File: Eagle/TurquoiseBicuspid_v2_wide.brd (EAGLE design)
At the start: 56 x 56 mm, 19 parts, among them J0 0Ω, J2 0Ω

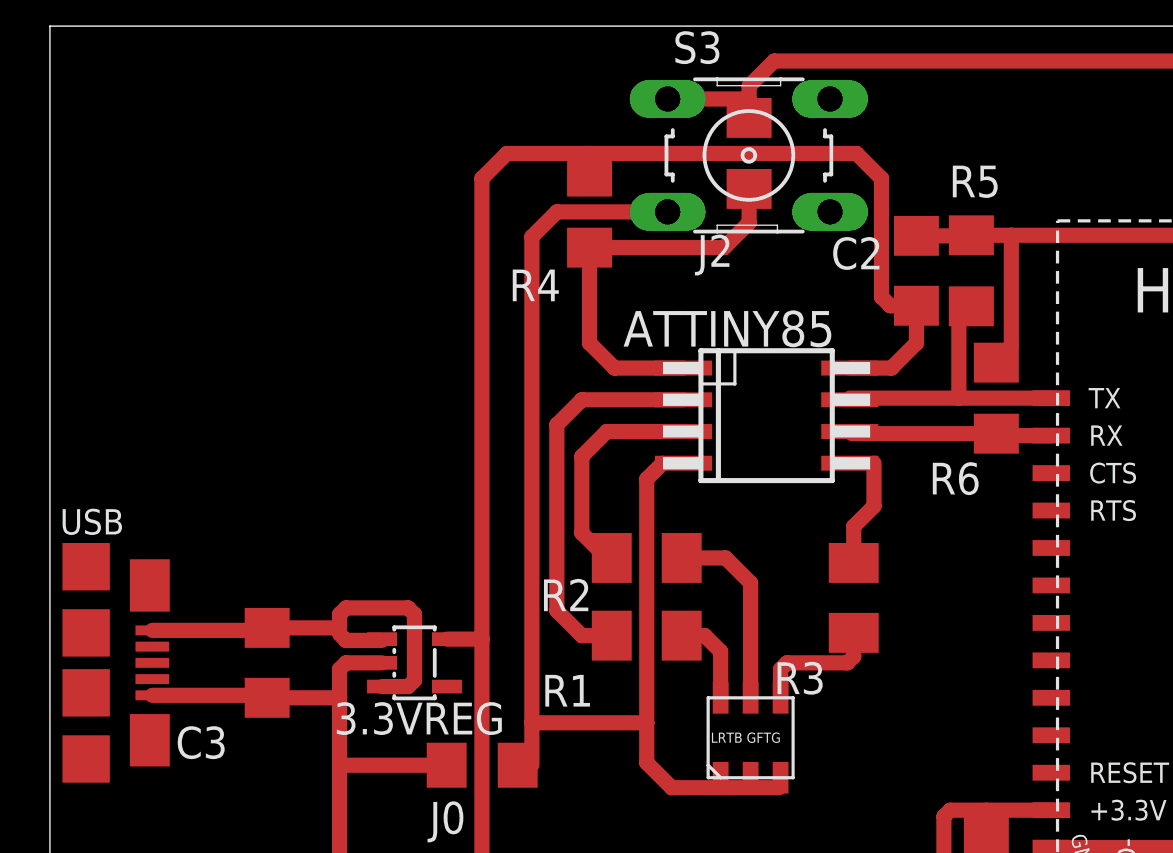
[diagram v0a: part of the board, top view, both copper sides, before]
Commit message: .6mm to .4mm usb
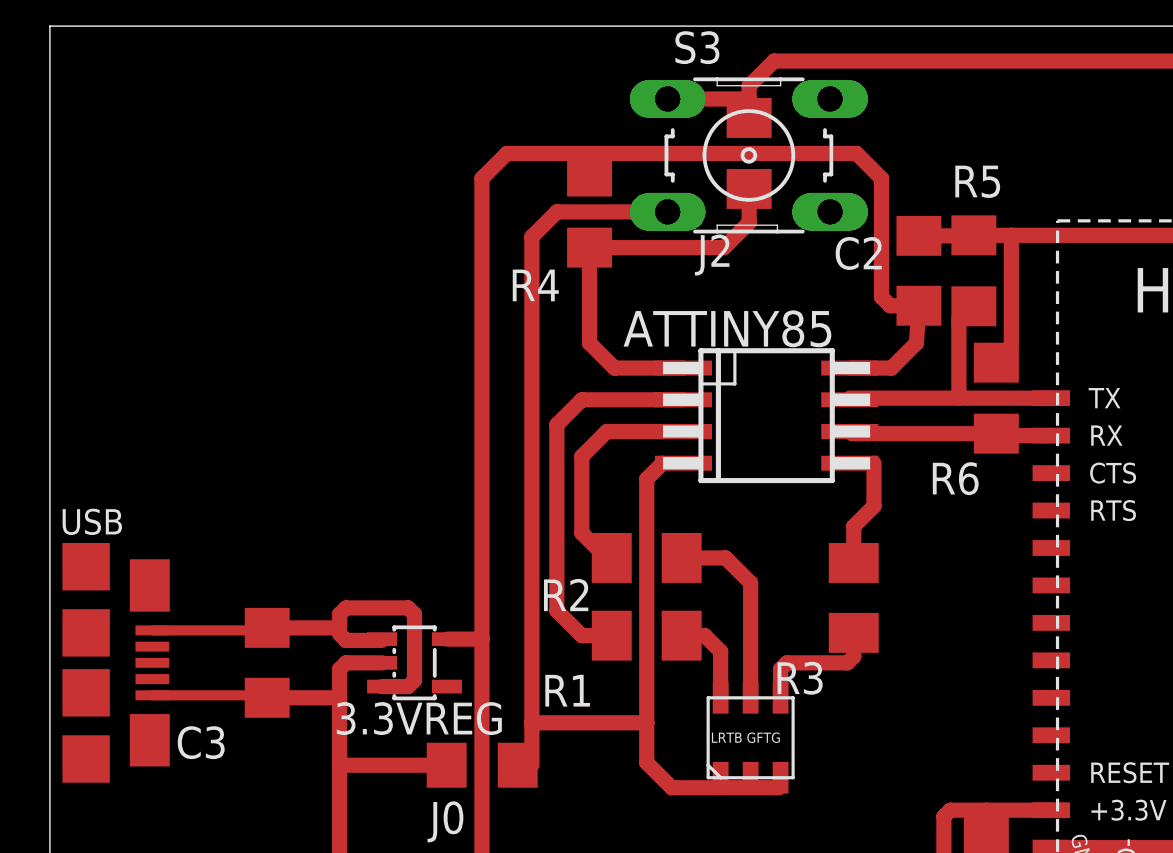
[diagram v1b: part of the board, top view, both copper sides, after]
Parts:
- moved R5 0.10 mm to (37.0, 46.2)
- moved C2 0.10 mm to (34.8, 46.2)
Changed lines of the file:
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@@
 </class>
 </classes>
-<designrules name="default">
+<designrules name="default *">
 <description language="de">&lt;b&gt;EAGLE Design Rules&lt;/b&gt;
 &lt;p&gt;
@@
 <param name="mtCopper" value="0.035mm 0.035mm 0.035mm 0.035mm 0.035mm 0.035mm 0.035mm 0.035mm 0.035mm 0.035mm 0.035mm 0.035mm 0.035mm 0.035mm 0.035mm 0.035mm"/>
 <param name="mtIsolate" value="1.5mm 0.15mm 0.2mm 0.15mm 0.2mm 0.15mm 0.2mm 0.15mm 0.2mm 0.15mm 0.2mm 0.15mm 0.2mm 0.15mm 0.2mm"/>
-<param name="mdWireWire" value="8mil"/>
-<param name="mdWirePad" value="8mil"/>
-<param name="mdWireVia" value="8mil"/>
-<param name="mdPadPad" value="8mil"/>
-<param name="mdPadVia" value="8mil"/>
-<param name="mdViaVia" value="8mil"/>
-<param name="mdSmdPad" value="8mil"/>
-<param name="mdSmdVia" value="8mil"/>
-<param name="mdSmdSmd" value="8mil"/>
+<param name="mdWireWire" value="10mil"/>
+<param name="mdWirePad" value="10mil"/>
+<param name="mdWireVia" value="10mil"/>
+<param name="mdPadPad" value="10mil"/>
+<param name="mdPadVia" value="10mil"/>
+<param name="mdViaVia" value="10mil"/>
+<param name="mdSmdPad" value="10mil"/>
+<param name="mdSmdVia" value="10mil"/>
+<param name="mdSmdSmd" value="10mil"/>
 <param name="mdViaViaSameLayer" value="8mil"/>
 <param name="mnLayersViaInSmd" value="2"/>
@@
 <attribute name="VALUE" x="29.87" y="47.64" size="1.27" layer="27" rot="R180"/>
 </element>
-<element name="R5" library="resistor" package="R1206" value="10kΩ" x="36.9" y="46.2" smashed="yes" rot="R270">
-<attribute name="NAME" x="36.003" y="49.143" size="1.27" layer="25"/>
-<attribute name="VALUE" x="38.403" y="49.187" size="1.27" layer="27"/>
+<element name="R5" library="resistor" package="R1206" value="10kΩ" x="37" y="46.2" smashed="yes" rot="R270">
+<attribute name="NAME" x="36.103" y="49.143" size="1.27" layer="25"/>
+<attribute name="VALUE" x="38.503" y="49.187" size="1.27" layer="27"/>
 </element>
 <element name="R6" library="resistor" package="R1206" value="10kΩ" x="37.9" y="41.1" smashed="yes" rot="R270">
@@
 <attribute name="VALUE" x="21.56" y="36.2042" size="1.4224" layer="27" ratio="9"/>
 </element>
-<element name="C2" library="rcl" package="C1206" value="0.1µf" x="34.7" y="46.2" smashed="yes" rot="R90">
-<attribute name="NAME" x="33.37" y="47.53" size="1.27" layer="25" rot="R180"/>
-<attribute name="VALUE" x="33.77" y="46.14" size="1.27" layer="27" rot="R180"/>
+<element name="C2" library="rcl" package="C1206" value="0.1µf" x="34.8" y="46.2" smashed="yes" rot="R90">
+<attribute name="NAME" x="33.47" y="47.53" size="1.27" layer="25" rot="R180"/>
+<attribute name="VALUE" x="33.87" y="46.14" size="1.27" layer="27" rot="R180"/>
 </element>
 <element name="C3" library="rcl" package="C1206" value="10µf" x="8.7" y="30.5" smashed="yes" rot="R270">
@@
 <contactref element="USB" pad="1"/>
 <contactref element="C3" pad="1"/>
-<wire x1="4.1" y1="31.8" x2="8.6" y2="31.8" width="0.6096" layer="1"/>
+<wire x1="4.1" y1="31.8" x2="8.6" y2="31.8" width="0.4064" layer="1"/>
 <wire x1="8.6" y1="31.8" x2="8.7" y2="31.9" width="0.4064" layer="1"/>
 <wire x1="8.7" y1="31.9" x2="11.6" y2="31.9" width="0.6096" layer="1"/>
@@
 <contactref element="R6" pad="1"/>
 <contactref element="R5" pad="1"/>
-<wire x1="4.1" y1="29.2" x2="8.6" y2="29.2" width="0.6096" layer="1"/>
+<wire x1="4.1" y1="29.2" x2="8.6" y2="29.2" width="0.4064" layer="1"/>
 <wire x1="8.6" y1="29.2" x2="8.7" y2="29.1" width="0.4064" layer="1"/>
 <wire x1="8.7" y1="29.1" x2="11.6" y2="29.1" width="0.6096" layer="1"/>
@@
 <wire x1="6.4" y1="4.1" x2="42.593528125" y2="4.1" width="0.6096" layer="1"/>
 <wire x1="38.4" y1="43.122" x2="38.5" y2="43.222" width="0.4064" layer="1"/>
-<wire x1="34.7" y1="47.6" x2="36.878" y2="47.6" width="0.6096" layer="1"/>
-<wire x1="36.878" y1="47.6" x2="36.9" y2="47.622" width="0.4064" layer="1"/>
-<wire x1="36.9" y1="47.622" x2="38.5" y2="47.622" width="0.6096" layer="1"/>
+<wire x1="34.8" y1="47.6" x2="36.878" y2="47.6" width="0.6096" layer="1"/>
+<wire x1="36.878" y1="47.6" x2="37" y2="47.622" width="0.4064" layer="1"/>
+<wire x1="37" y1="47.622" x2="38.5" y2="47.622" width="0.6096" layer="1"/>
 <wire x1="38.5" y1="43.222" x2="38.5" y2="47.622" width="0.6096" layer="1"/>
 <wire x1="23.9" y1="28.1" x2="23.9" y2="26.5" width="0.6096" layer="1"/>
@@
 <wire x1="17.3" y1="49.9" x2="18.3" y2="50.9" width="0.6096" layer="1"/>
 <wire x1="18.3" y1="50.9" x2="21.61" y2="50.9" width="0.6096" layer="1"/>
-<wire x1="34.7" y1="44.8" x2="34.7" y2="43.305" width="0.6096" layer="1"/>
+<wire x1="34.8" y1="44.8" x2="34.7" y2="43.305" width="0.6096" layer="1"/>
 <wire x1="34.7" y1="43.305" x2="33.7" y2="42.305" width="0.6096" layer="1"/>
 <wire x1="33.7" y1="42.305" x2="32.03" y2="42.305" width="0.6096" layer="1"/>
@@
 <wire x1="33.3" y1="49.9" x2="33.3" y2="45.154" width="0.6096" layer="1"/>
 <wire x1="33.3" y1="45.154" x2="33.654" y2="44.8" width="0.6096" layer="1"/>
-<wire x1="33.654" y1="44.8" x2="34.7" y2="44.8" width="0.6096" layer="1"/>
+<wire x1="33.654" y1="44.8" x2="34.8" y2="44.8" width="0.6096" layer="1"/>
 <wire x1="21.61" y1="49.972" x2="21.61" y2="50.9" width="0.4064" layer="1"/>
 <wire x1="35.8" y1="22.4" x2="35.8" y2="24.346" width="0.6096" layer="1"/>
@@
 <wire x1="36.4" y1="41.1" x2="32.03" y2="41.1" width="0.6096" layer="1"/>
 <wire x1="32.03" y1="41.1" x2="32.03" y2="41.035" width="0.4064" layer="1"/>
-<wire x1="36.9" y1="44.778" x2="36.4" y2="44.278" width="0.4064" layer="1"/>
+<wire x1="37" y1="44.778" x2="36.4" y2="44.278" width="0.4064" layer="1"/>
 <wire x1="36.4" y1="44.278" x2="36.4" y2="41.1" width="0.6096" layer="1"/>
 </signal>
